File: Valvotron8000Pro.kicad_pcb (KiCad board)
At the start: 2 copper layers, 99.7 x 99.9 mm, 132 parts, among them J1 USB_B_Micro, J10 SMA_P2, J11 SMA_P3, J12 Sens. P2, J13 Sens. P3, J14 Servo1, J15 SWD, J16 Servo2, J17 Sens. P1, J18 24V_OUT_TO_BEC, J19 BEC_8V4_IN, J2 Conn_01x02, J20 M12_P2, J3 CAN_OUT, J4 CAN_IN, J5 PWR SUPPLY, J6 M12_P3, J7 M12_P1, J9 SMA_P1, U1 NCP1117-3.3_SOT223, U10 PCA9548APW, U2 W25Q128JVS, U3 RP2040, U4 MCP2515-xST, U5 MCP2551-I-SN, U6 TSR1-2450E, U7 ADS8681IPW, U8 ADS8681IPW, U9 ADS8681IPW, Y1 ABM8-272-T3, Y3 Crystal_GND24

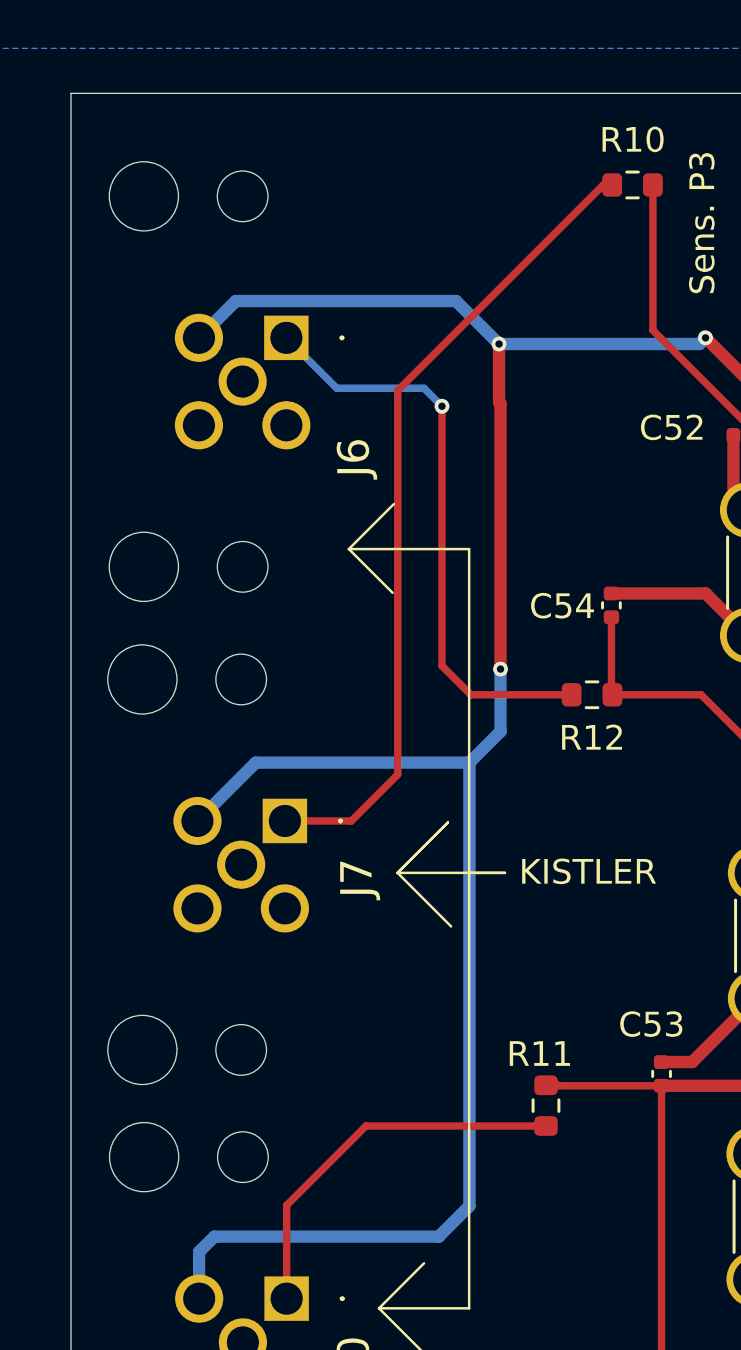
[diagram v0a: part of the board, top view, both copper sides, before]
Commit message: added silkscreen indicator for software
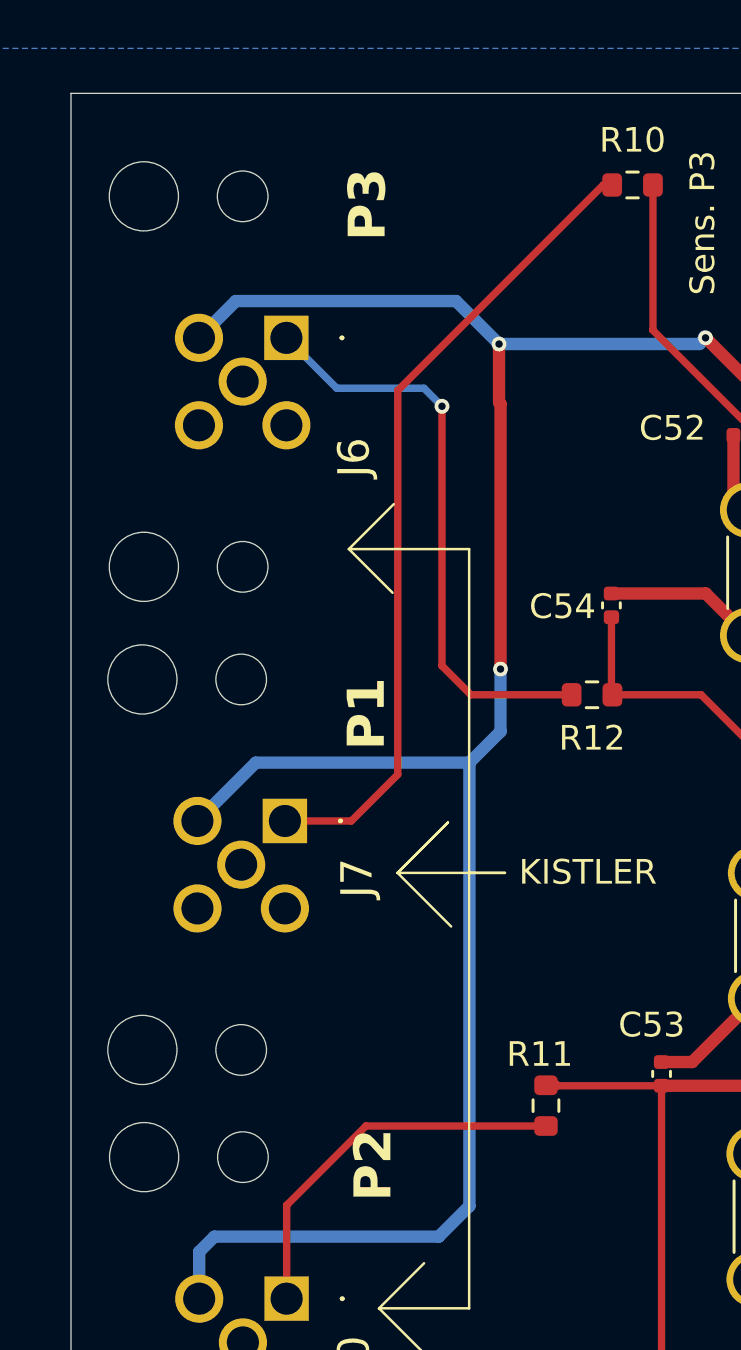
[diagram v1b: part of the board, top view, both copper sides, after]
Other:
- board text added: "P1"
- board text added: "P2"
- board text added: "P3"
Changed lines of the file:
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@@
+		)
+	)
+	(gr_text "P3\n\n"
+		(at 84.83 49.56 90)
+		(layer "F.SilkS")
+		(effects
+			(font
+				(face "Agency FB")
+				(size 1.5 1.5)
+				(thickness 0.3)
+				(bold yes)
+			)
+			(justify left bottom)
+		)
+		(render_cache "P3\n\n" 90
+			(polygon
+				(pts
+					(xy 81.403789 48.698434) (xy 81.44142 48.723985) (xy 81.465423 48.767123) (xy 81.474678 48.835514)
+					(xy 81.474678 49.22386) (xy 82.055 49.22386) (xy 82.055 49.463646) (xy 80.448859 49.463646) (xy 80.448859 49.22386)
+					(xy 80.654023 49.22386) (xy 81.269515 49.22386) (xy 81.269515 48.93086) (xy 80.654023 48.93086)
+					(xy 80.654023 49.22386) (xy 80.448859 49.22386) (xy 80.448859 48.835514) (xy 80.458114 48.767123)
+					(xy 80.482117 48.723985) (xy 80.519748 48.698434) (xy 80.575895 48.68906) (xy 81.347642 48.68906)
+				)
+			)
+			(polygon
+				(pts
+					(xy 81.927963 47.739719) (xy 81.984267 47.749024) (xy 82.021888 47.774323) (xy 82.0458 47.81688)
+					(xy 82.055 47.884158) (xy 82.055 48.376002) (xy 82.045857 48.442167) (xy 82.022037 48.484143) (xy 81.984426 48.50919)
+					(xy 81.927963 48.518426) (xy 81.539159 48.518426) (xy 81.539159 48.282762) (xy 81.849836 48.282762)
+					(xy 81.849836 47.974375) (xy 81.446468 47.974375) (xy 81.244327 48.268474) (xy 81.194043 48.268474)
+					(xy 80.9941 47.974375) (xy 80.654023 47.974375) (xy 80.654023 48.282762) (xy 80.947114 48.282762)
+					(xy 80.947114 48.518426) (xy 80.575895 48.518426) (xy 80.51967 48.509086) (xy 80.482044 48.483661)
+					(xy 80.458086 48.440814) (xy 80.448859 48.372979) (xy 80.448859 47.884158) (xy 80.458058 47.81688)
+					(xy 80.48197 47.774323) (xy 80.519591 47.749024) (xy 80.575895 47.739719) (xy 80.971477 47.739719)
+					(xy 81.031884 47.748801) (xy 81.081004 47.774988) (xy 81.121687 47.819678) (xy 81.219689 47.968238)
+					(xy 81.315676 47.817571) (xy 81.353777 47.774377) (xy 81.401751 47.748742) (xy 81.462863 47.739719)
+				)
+			)
 		)
 	)
@@
 		)
 	)
+	(gr_text "P2\n\n"
+		(at 85.06 88.45 90)
+		(layer "F.SilkS")
+		(effects
+			(font
+				(face "Agency FB")
+				(size 1.5 1.5)
+				(thickness 0.3)
+				(bold yes)
+			)
+			(justify left bottom)
+		)
+		(render_cache "P2\n\n" 90
+			(polygon
+				(pts
+					(xy 81.633789 87.588434) (xy 81.67142 87.613985) (xy 81.695423 87.657123) (xy 81.704678 87.725514)
+					(xy 81.704678 88.11386) (xy 82.285 88.11386) (xy 82.285 88.353646) (xy 80.678859 88.353646) (xy 80.678859 88.11386)
+					(xy 80.884023 88.11386) (xy 81.499515 88.11386) (xy 81.499515 87.82086) (xy 80.884023 87.82086)
+					(xy 80.884023 88.11386) (xy 80.678859 88.11386) (xy 80.678859 87.725514) (xy 80.688114 87.657123)
+					(xy 80.712117 87.613985) (xy 80.749748 87.588434) (xy 80.805895 87.57906) (xy 81.577642 87.57906)
+				)
+			)
+			(polygon
+				(pts
+					(xy 81.136356 86.655364) (xy 81.185743 86.66055) (xy 81.24126 86.677221) (xy 81.304426 86.707663)
+					(xy 82.073974 87.148216) (xy 82.073974 86.657379) (xy 82.285 86.657379) (xy 82.285 87.435079) (xy 82.135523 87.435079)
+					(xy 81.180503 86.892035) (xy 80.884023 86.892035) (xy 80.884023 87.184028) (xy 81.182976 87.184028)
+					(xy 81.182976 87.418684) (xy 80.805895 87.418684) (xy 80.749755 87.409307) (xy 80.712124 87.383745)
+					(xy 80.688117 87.340581) (xy 80.678859 87.272138) (xy 80.678859 86.801818) (xy 80.688114 86.733427)
+					(xy 80.712117 86.690289) (xy 80.749748 86.664738) (xy 80.805895 86.655364)
+				)
+			)
+		)
+	)
 	(gr_text "SMA P1"
 		(at 103.67 60.23 270)
@@
 		)
 	)
+	(gr_text "P1\n\n"
+		(at 84.79 70.18 90)
+		(layer "F.SilkS")
+		(effects
+			(font
+				(face "Agency FB")
+				(size 1.5 1.5)
+				(thickness 0.3)
+				(bold yes)
+			)
+			(justify left bottom)
+		)
+		(render_cache "P1\n\n" 90
+			(polygon
+				(pts
+					(xy 81.363789 69.318434) (xy 81.40142 69.343985) (xy 81.425423 69.387123) (xy 81.434678 69.455514)
+					(xy 81.434678 69.84386) (xy 82.015 69.84386) (xy 82.015 70.083646) (xy 80.408859 70.083646) (xy 80.408859 69.84386)
+					(xy 80.614023 69.84386) (xy 81.229515 69.84386) (xy 81.229515 69.55086) (xy 80.614023 69.55086)
+					(xy 80.614023 69.84386) (xy 80.408859 69.84386) (xy 80.408859 69.455514) (xy 80.418114 69.387123)
+					(xy 80.442117 69.343985) (xy 80.479748 69.318434) (xy 80.535895 69.30906) (xy 81.307642 69.30906)
+				)
+			)
+			(polygon
+				(pts
+					(xy 82.015 68.848449) (xy 82.015 69.084112) (xy 80.877805 69.084112) (xy 80.877805 69.176345) (xy 80.845565 69.176345)
+					(xy 80.408859 69.052422) (xy 80.408859 68.848449)
+				)
+			)
+		)
+	)

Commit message: added reset and bootsel buttons
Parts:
- added BOOTSEL: SW_Push, Button_Switch_SMD:SW_SPST_B3U-1000P, F.Cu at (147.9, 77.8)
- added RESET: SW_Push, Button_Switch_SMD:SW_SPST_B3U-1000P, F.Cu at (141.8, 135.4)
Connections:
- U3 pad 9: /RP2040_integration/GPIO7 -> SS
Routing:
- net AIN1_GND: track 384.2 -> 400.2 mm, vias 16 -> 20
- net /RP2040_integration/QSPI_SS: track 81.8 -> 86.8 mm
- net Net-(U3-RUN): track 16.9 -> 18.6 mm
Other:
- board text added: "BOOTSEL"

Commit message: last modifications
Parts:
- renumbered BOOTSEL to BOOTSEL1, RESET to RESET1
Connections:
- J10 pad 2: AGND -> AIN1_GND
- J11 pad 2: AGND -> AIN1_GND
- J9 pad 2: AGND -> AIN1_GND
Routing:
- net AGND: track 81.9 -> 53.0 mm
- net AIN1_GND: track 400.2 -> 423.8 mm, vias 20 -> 22

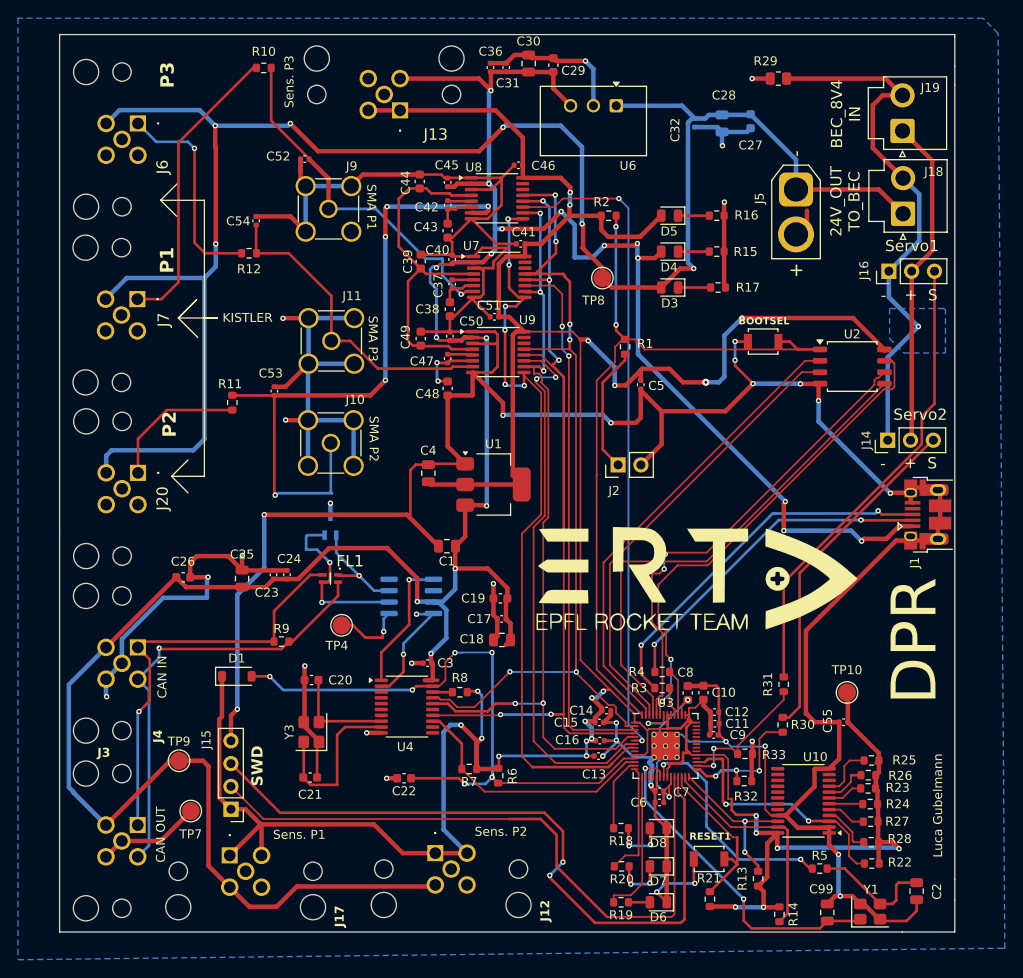
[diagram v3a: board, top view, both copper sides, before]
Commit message: Changed M12 for SMA + 2 pins alim. --> we will have to split the cable from Kistlers
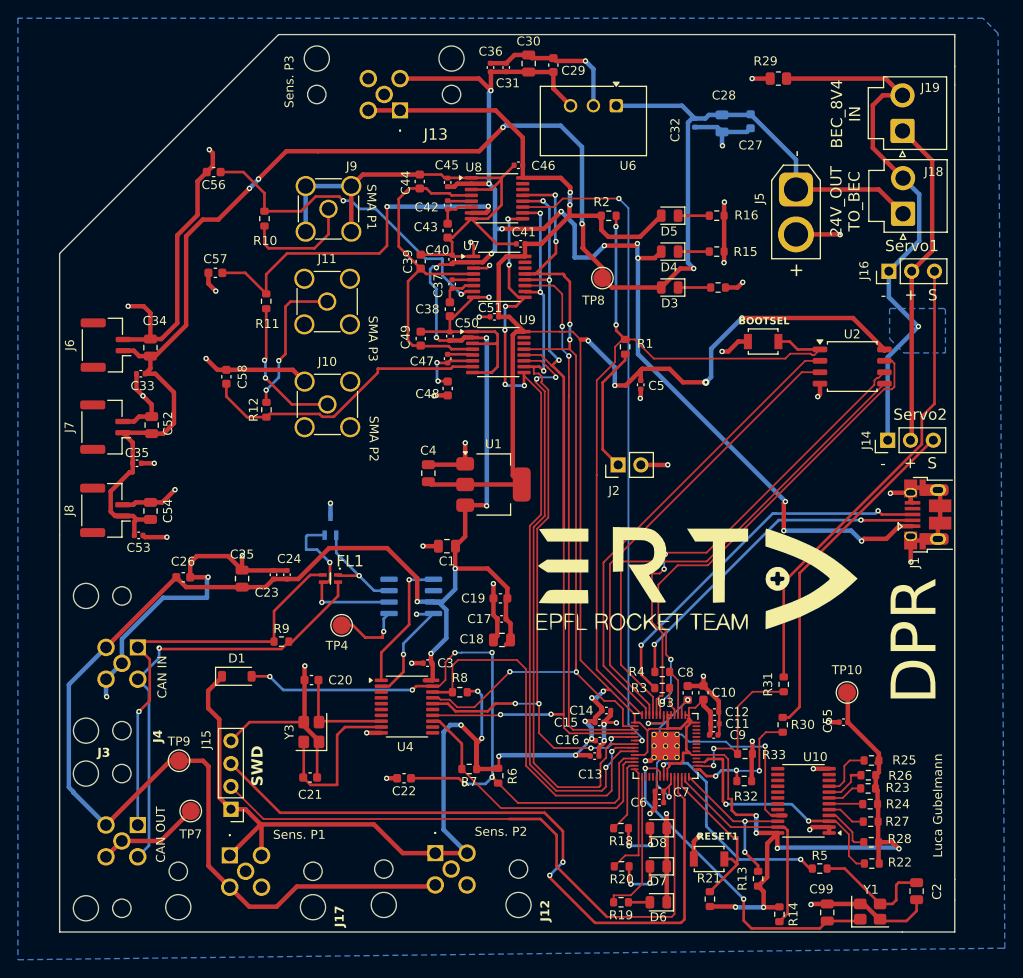
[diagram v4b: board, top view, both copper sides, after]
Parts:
- removed J20: M12_P2, KiNic_footprints:M12B05PFFREE0001
- added C33: 100n, Capacitor_SMD:C_0402_1005Metric, F.Cu at (78.6, 81.4)
- added C34: 10u, Capacitor_SMD:C_0805_2012Metric, F.Cu at (79.6, 78.4)
- added C35: 100n, Capacitor_SMD:C_0402_1005Metric, F.Cu at (78.2, 91.3)
- added C56: 1n, Capacitor_SMD:C_0603_1608Metric, F.Cu at (86.7, 58.9)
- added C57: 1n, Capacitor_SMD:C_0603_1608Metric, F.Cu at (86.9, 70.1)
- added C58: 1n, Capacitor_SMD:C_0603_1608Metric, F.Cu at (88.1, 81.7)
- added J8: PWR_K3, Connector_JST:JST_GH_BM02B-GHS-TBT_1x02-1MP_P1.25mm_Vertical, F.Cu at (74.6, 96.6)
- C52, C54: value 4.7n -> 10u; footprint Capacitor_SMD:C_0402_1005Metric -> Capacitor_SMD:C_0805_2012Metric
- C53: value 4.7n -> 100n
- J10: value SMA_P2 -> SMA_K2
- J11: value SMA_P3 -> SMA_K3
- J6: value M12_P3 -> PWR_K1; footprint KiNic_footprints:M12B05PFFREE0001 -> Connector_JST:JST_GH_BM02B-GHS-TBT_1x02-1MP_P1.25mm_Vertical
- J7: value M12_P1 -> PWR_K2; footprint KiNic_footprints:M12B05PFFREE0001 -> Connector_JST:JST_GH_BM02B-GHS-TBT_1x02-1MP_P1.25mm_Vertical
- J9: value SMA_P1 -> SMA_K1
- moved C54 34.4 mm to (79.7, 96.6), turned to 90 degrees
- moved C52 34.2 mm to (79.8, 87.1), turned to 90 degrees
- moved J6 24.9 mm to (74.7, 78.2), turned to 90 degrees
- moved C53 22.1 mm to (78.3, 99.4), turned to 0 degrees
- moved R12 17.5 mm to (92.6, 85.4), turned to 90 degrees
- moved R10 16.8 mm to (92.3, 64.1), turned to -90 degrees
- moved J7 14.7 mm to (74.6, 87.3), turned to 90 degrees
- moved R11 11.9 mm to (92.5, 73.3), turned to -90 degrees
- moved J11 4.40 mm to (99.3, 73.3)
- moved J10 4.32 mm to (99.3, 84.8)
- moved C13 0.43 mm to (129.1, 123.9)
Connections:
- BOOTSEL1 pad 1: AIN1_GND -> GND
- C1 pad 2: AIN1_GND -> GND
- C10 pad 2: AIN1_GND -> GND
- C11 pad 2: AIN1_GND -> GND
- C12 pad 2: AIN1_GND -> GND
- C13 pad 2: AIN1_GND -> GND
- C14 pad 2: AIN1_GND -> GND
- C15 pad 2: AIN1_GND -> GND
- C16 pad 2: AIN1_GND -> GND
- C2 pad 2: AIN1_GND -> GND
- C38 pad 1: AIN1_GND -> GND
- C39 pad 2: AIN1_GND -> GND
- C4 pad 2: AIN1_GND -> GND
- C40 pad 2: AIN1_GND -> GND
- C41 pad 1: AIN1_GND -> GND
- C43 pad 1: AIN1_GND -> GND
- C44 pad 2: AIN1_GND -> GND
- C45 pad 2: AIN1_GND -> GND
- C46 pad 1: AIN1_GND -> GND
- C48 pad 1: AIN1_GND -> GND
- C49 pad 2: AIN1_GND -> GND
- C5 pad 2: AIN1_GND -> GND
- C50 pad 2: AIN1_GND -> GND
- C51 pad 1: AIN1_GND -> GND
- C52 pad 1: AGND -> +24V
- C52 pad 2: AIN1_P -> GND
- C53 pad 1: AGND -> +24V
- C53 pad 2: AIN2_P -> GND
- C54 pad 1: AGND -> +24V
- C54 pad 2: AIN3_P -> GND
- C55 pad 1: AIN1_GND -> GND
- C6 pad 2: AIN1_GND -> GND
- C7 pad 2: AIN1_GND -> GND
- C8 pad 2: AIN1_GND -> GND
- C9 pad 2: AIN1_GND -> GND
- C99 pad 2: AIN1_GND -> GND
- D6 pad 1: AIN1_GND -> GND
- D7 pad 1: AIN1_GND -> GND
- D8 pad 1: AIN1_GND -> GND
- J1 pad 5: AIN1_GND -> GND
- J1 pad 6: AIN1_GND -> GND
- J10 pad 1: AIN2_P -> Net-(J10-In)
- J10 pad 2: AIN1_GND -> GND
- J11 pad 1: AIN3_P -> Net-(J11-In)
- J11 pad 2: AIN1_GND -> GND
- J15 pad 4: AIN1_GND -> GND
- J2 pad 2: AIN1_GND -> GND
- J6 pad 1: P3_OUT -> +24V
- J6 pad 2: unconnected-(J6-Pad2) -> GND
- J7 pad 1: P1_OUT -> +24V
- J7 pad 2: unconnected-(J7-Pad2) -> GND
- J9 pad 1: AIN1_P -> Net-(J9-In)
- J9 pad 2: AIN1_GND -> GND
- R10 pad 1: P1_OUT -> AIN1_P
- R10 pad 2: AIN1_P -> Net-(J9-In)
- R11 pad 1: P2_OUT -> AIN2_P
- R11 pad 2: AIN2_P -> Net-(J10-In)
- R12 pad 1: P3_OUT -> AIN3_P
- R12 pad 2: AIN3_P -> Net-(J11-In)
- RESET1 pad 1: AIN1_GND -> GND
- U1 pad 1: AIN1_GND -> GND
- U10 pad 1: AIN1_GND -> GND
- U10 pad 12: AIN1_GND -> GND
- U10 pad 2: AIN1_GND -> GND
- U10 pad 21: AIN1_GND -> GND
- U2 pad 4: AIN1_GND -> GND
- U3 pad 19: AIN1_GND -> GND
- U3 pad 57: AIN1_GND -> GND
- U7 pad 1: AIN1_GND -> GND
- U7 pad 3: AIN1_GND -> GND
- U7 pad 8: AIN1_GND -> GND
- U8 pad 1: AIN1_GND -> GND
- U8 pad 3: AIN1_GND -> GND
- U8 pad 8: AIN1_GND -> GND
- U9 pad 1: AIN1_GND -> GND
- U9 pad 3: AIN1_GND -> GND
- U9 pad 8: AIN1_GND -> GND
- Y1 pad 2: AIN1_GND -> GND
- Y1 pad 4: AIN1_GND -> GND
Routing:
- net AIN1_GND: track 423.8 -> 0.00 mm, vias 22 -> 0
- net GND: track 119.4 -> 411.5 mm, vias 15 -> 51
- net AGND: track 53.0 -> 0.00 mm
- net SS: track 2.21 -> 42.3 mm
- net AIN2_P: track 74.2 -> 40.9 mm, vias 5 -> 2
- net P1_OUT: track 33.0 -> 0.00 mm
- net P3_OUT: track 23.7 -> 0.00 mm, vias 1 -> 0
- net +24V: track 202.8 -> 186.0 mm, vias 6 -> 5
- net Net-(J11-In): track 0.00 -> 16.4 mm, vias 0 -> 2
- net Net-(J10-In): track 0.00 -> 15.9 mm, vias 0 -> 2
- net P2_OUT: track 15.6 -> 0.00 mm
- net Net-(J9-In): track 0.00 -> 12.8 mm
- net CS_ADC3: track 61.1 -> 66.8 mm
- net RESET_CAN: track 71.1 -> 75.2 mm
- net INT: track 28.8 -> 32.6 mm
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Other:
- outline, holes or cut-outs redrawn
- board text removed: "KISTLER"
- board text removed: "P1"
- board text removed: "P2"
- board text removed: "P3"

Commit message: Dernières modifs
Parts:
- added H1: MountingHole, MountingHole:MountingHole_2.5mm, F.Cu at (73.2, 69.3)
- added H2: MountingHole, MountingHole:MountingHole_2.5mm, F.Cu at (164.6, 47.4)
- added H4: MountingHole, MountingHole:MountingHole_2.5mm, F.Cu at (165.3, 139.8)
- J18, J19: footprint Connector_JST:JST_VH_B2P-VH_1x02_P3.96mm_Vertical -> Connector_JST:JST_XH_B2B-XH-AM_1x02_P2.50mm_Vertical
- J6, J7, J8: footprint Connector_JST:JST_GH_BM02B-GHS-TBT_1x02-1MP_P1.25mm_Vertical -> Connector_JST:JST_XH_B2B-XH-AM_1x02_P2.50mm_Vertical
- moved J13 82.9 mm to (108.2, 135.0), turned to 0 degrees
- moved J12 81.3 mm to (106.5, 53.6), turned to 180 degrees
- moved C2 40.6 mm to (126.5, 125.9), turned to 180 degrees
- moved Y1 33.7 mm to (127.3, 132.2)
- moved R5 33.4 mm to (121.9, 128.0)
- moved C99 26.8 mm to (128.7, 136.3)
- moved C35 8.90 mm to (79.8, 82.6)
- moved C53 7.12 mm to (80.1, 92.5)
- moved C33 4.11 mm to (82.2, 79.4), turned to 0 degrees
- moved R14 2.86 mm to (147.0, 140.6), turned to 0 degrees
- moved J16 2.79 mm to (161.9, 72.7)
- moved J19 2.70 mm to (163.4, 57.0)
- moved J18 2.70 mm to (163.4, 66.2)
- moved R29 2.51 mm to (152.1, 48.5)
- moved R23 0.45 mm to (159.9, 127.8)
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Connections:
- J12 pad 1: +3V3 -> PTE2_SCL
- J12 pad 2: +3V3 -> PTE2_SDA
- J13 pad 1: +3V3 -> PTE3_SCL
- J13 pad 2: +3V3 -> PTE3_SDA
- J17 pad 1: +3V3 -> PTE1_SCL
- J17 pad 2: +3V3 -> PTE1_SDA
- R24 pad 1: PTE2_SDA -> +3V3
- R24 pad 2: +3V3 -> PTE2_SDA
- R26 pad 1: PTE3_SDA -> +3V3
- R26 pad 2: +3V3 -> PTE3_SDA
- R28 pad 1: PTE1_SDA -> +3V3
- R28 pad 2: +3V3 -> PTE1_SDA
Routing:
- net PTE2_SDA: track 3.76 -> 162.6 mm, vias 0 -> 7
- net PTE2_SCL: track 3.95 -> 150.9 mm, vias 0 -> 5
- net PTE3_SCL: track 6.08 -> 105.9 mm, vias 0 -> 3
- net PTE1_SCL: track 4.36 -> 92.9 mm, vias 0 -> 5
- net PTE1_SDA: track 5.64 -> 78.8 mm, vias 0 -> 1
- net PTE3_SDA: track 4.80 -> 66.4 mm, vias 0 -> 3
- net +3V3: track 410.3 -> 367.7 mm, vias 22 -> 21
- net +24V: track 186.0 -> 207.1 mm
- net /RP2040_integration/XOUT: track 25.8 -> 45.0 mm
- net GND: track 411.5 -> 420.4 mm, vias 51 -> 54
- net /RP2040_integration/XIN: track 37.6 -> 30.1 mm
- net GND_SERVO: track 61.1 -> 54.2 mm
- net +5V: track 331.0 -> 335.1 mm
- net SWD: track 79.3 -> 82.4 mm
- net SWCLK: track 72.9 -> 75.7 mm
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- removed copper zone on B.Cu, net GND_SERVO
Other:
- board text added: "COPV"
- board text added: "ETH"
- board text added: "ETHANOL"
- board text added: "LOX"
- board text removed: "SMA P1"
- board text removed: "SMA P2"
- board text removed: "SMA P3"
- board text removed: "Servo1"
- board text removed: "Servo2"
